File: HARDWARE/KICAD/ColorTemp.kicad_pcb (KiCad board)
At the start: 2 copper layers, 27.5 x 27.5 mm, 26 parts, among them J1 POWER, J2 Conn_02x05_Odd_Even, SW1 USER, SW2 ~{RESET}, U1 CH32V003F4U6, U2 MCP9700A

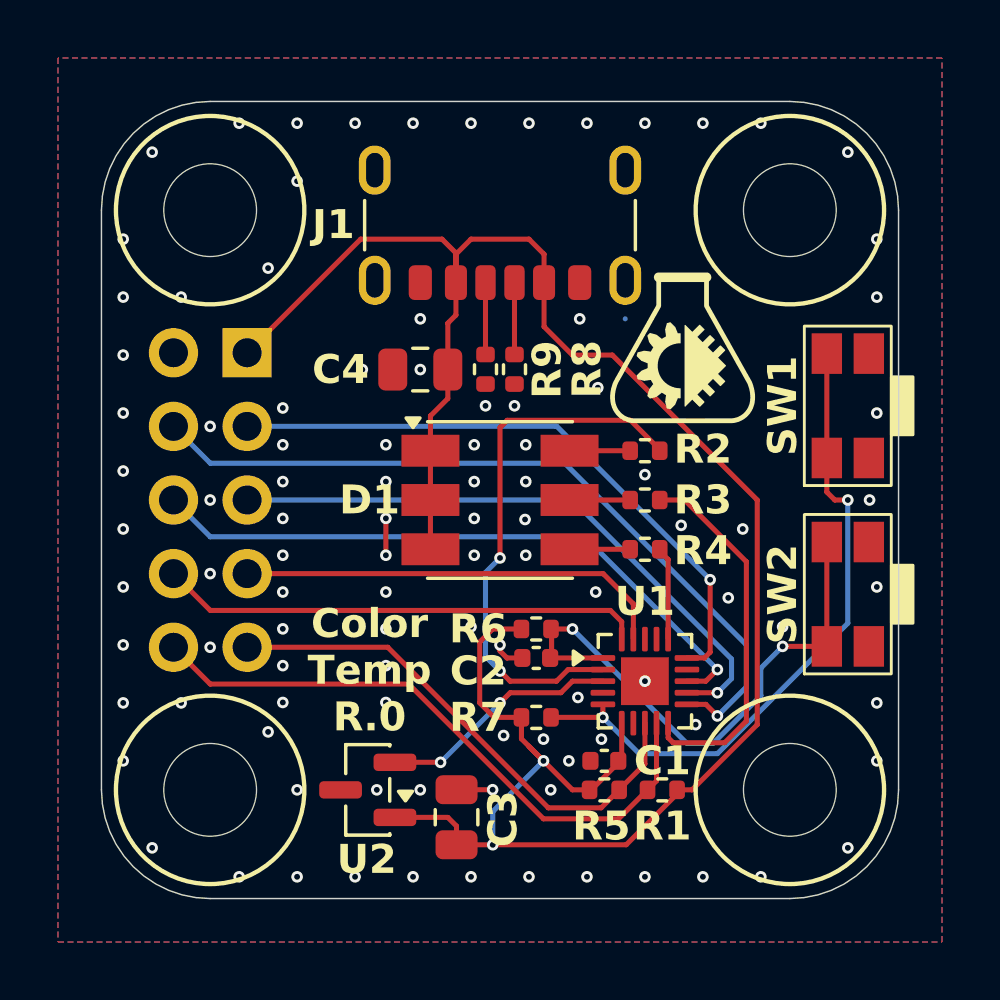
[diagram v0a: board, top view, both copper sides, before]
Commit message: Added fiducial marks.
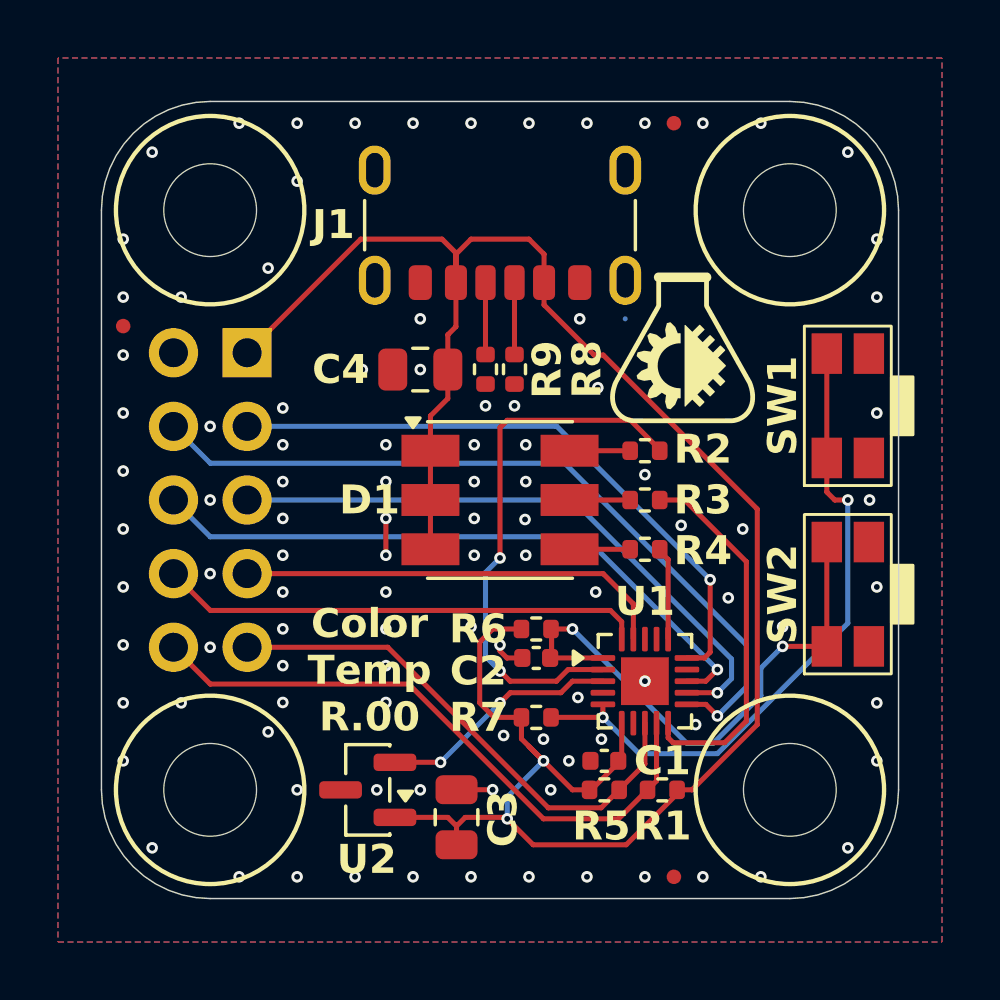
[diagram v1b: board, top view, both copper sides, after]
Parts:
- added FID1: Fiducial, ColorTemp:Fiducial_0.5mm_Mask1mm, F.Cu at (137.0, 94.0)
- added FID2: Fiducial, ColorTemp:Fiducial_0.5mm_Mask1mm, F.Cu at (156.0, 87.0)
- added FID3: Fiducial, ColorTemp:Fiducial_0.5mm_Mask1mm, F.Cu at (156.0, 113.0)
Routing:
- net +5V: track 75.8 -> 74.8 mm
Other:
- board text added: "Color Temp R.00"
- board text removed: "Color Temp R.0"

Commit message: Renumbering, PWR_FLAG, schematic detailing.
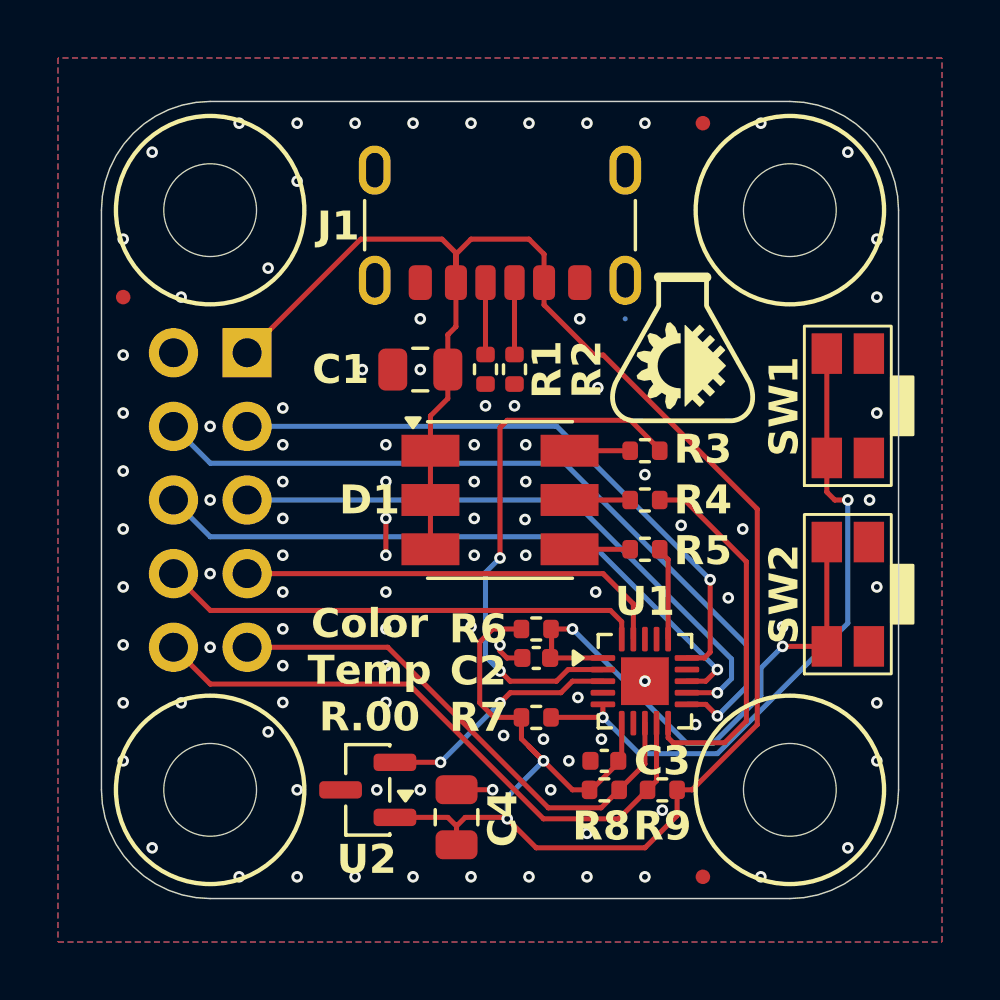
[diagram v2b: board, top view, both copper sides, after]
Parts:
- J2: value Conn_02x05_Odd_Even -> EXPANSION
- moved FID1 1.00 mm to (157.0, 87.0)
- moved FID2 1.00 mm to (137.0, 93.0)
- moved FID3 1.00 mm to (157.0, 113.0)
- moved G*** 0.57 mm to (153.8, 100.0), turned to -90 degrees
- renumbered C4 to C1, C1 to C3, C3 to C4, FID2 to FID1, FID1 to FID2, H3 to H1, H1 to H2, H4 to H3, H2 to H4, R9 to R1, R8 to R2, R2 to R3, R3 to R4, R4 to R5, R5 to R8, R1 to R9
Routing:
- net +5V: track 74.8 -> 75.3 mm
- net GND: vias 102 -> 101
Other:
- board text added: "C4 DIO"
- board text added: "C6 C5"
- board text added: "CL DA"
- board text added: "G 5V"
- board text added: "RX TX"
- board text removed: "5V G"
- board text removed: "C5 C6"
- board text removed: "DA CL"
- board text removed: "DIO C4"
- board text removed: "TX RX"

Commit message: Finished schematic.
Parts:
- R3, R4, R5: value 1K 1% -> 220R 1%
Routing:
- net GND: track 5.88 -> 5.79 mm, vias 101 -> 110
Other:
- board text added: "Mechatronix Lab Rev.00 2026.03.21"
- board text removed: "Mechatronix Lab Rev.00 2026.03.14"

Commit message: Finished Schematic and PCB Design.
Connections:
- net Net-(J1-CC1) renamed /CC1
- net Net-(J1-CC2) renamed /CC2
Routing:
- net GND: vias 110 -> 111
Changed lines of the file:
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@@
 	(net 18 "PC5")
 	(net 19 "USER")
-	(net 20 "Net-(J1-CC2)")
-	(net 21 "Net-(J1-CC1)")
+	(net 20 "/CC2")
+	(net 21 "/CC1")
 	(net 22 "unconnected-(U1-PD3-Pad17)")
 	(net 23 "unconnected-(U1-PC7-Pad14)")
@@
 			(end 2.5 -2.75)
 			(stroke
-				(width 0.1)
-				(type default)
+				(width 0.12)
+				(type solid)
 			)
 			(layer "F.SilkS")
@@
 		(fp_line
 			(start -2.5 2.75)
-			(end 2.5 2.75)
+			(end 3.65 2.75)
 			(stroke
-				(width 0.1)
-				(type default)
+				(width 0.12)
+				(type solid)
 			)
 			(layer "F.SilkS")
@@
 			)
 			(stroke
-				(width 0.1)
+				(width 0.12)
 				(type solid)
 			)
@@
 			)
 			(stroke
-				(width 0.1)
+				(width 0.12)
 				(type solid)
 			)
@@
 			)
 			(stroke
-				(width 0.1)
+				(width 0.12)
 				(type solid)
 			)
@@
 		(property "Reference" "SW2"
 			(at 0 -2.2 90)
-			(layer "F.SilkS" knockout)
+			(layer "F.SilkS")
 			(effects
 				(font
@@
 			(end 2.75 1.5)
 			(stroke
-				(width 0.1)
-				(type default)
+				(width 0.12)
+				(type solid)
 			)
 			(fill no)
@@
 		(property "Reference" "SW1"
 			(at -0.025 -2.2 90)
-			(layer "F.SilkS" knockout)
+			(layer "F.SilkS")
 			(effects
 				(font
@@
 			(end 2.75 1.5)
 			(stroke
-				(width 0.1)
-				(type default)
+				(width 0.12)
+				(type solid)
 			)
 			(fill no)
@@
 			(at 5.58 -1.13 0)
 			(unlocked yes)
-			(layer "F.SilkS" knockout)
+			(layer "F.SilkS")
 			(effects
 				(font
@@
 			(layers "F.Cu" "F.Mask" "F.Paste")
 			(roundrect_rratio 0.25)
-			(net 21 "Net-(J1-CC1)")
+			(net 21 "/CC1")
 			(pinfunction "CC1")
 			(pintype "bidirectional")
@@
 			(layers "F.Cu" "F.Mask" "F.Paste")
 			(roundrect_rratio 0.25)
-			(net 20 "Net-(J1-CC2)")
+			(net 20 "/CC2")
 			(pinfunction "CC2")
 			(pintype "bidirectional")
@@
 			(layers "F.Cu" "F.Mask" "F.Paste")
 			(roundrect_rratio 0.25)
-			(net 20 "Net-(J1-CC2)")
+			(net 20 "/CC2")
 			(pintype "passive")
 		)
@@
 			(end 3.25 0)
 			(stroke
-				(width 0.15)
+				(width 0.12)
 				(type solid)
 			)
@@
 			(layers "F.Cu" "F.Mask" "F.Paste")
 			(roundrect_rratio 0.25)
-			(net 21 "Net-(J1-CC1)")
+			(net 21 "/CC1")
 			(pintype "passive")
 		)
@@
 			(end 3.25 0)
 			(stroke
-				(width 0.15)
+				(width 0.12)
 				(type solid)
 			)
@@
 			(end 3.25 0)
 			(stroke
-				(width 0.15)
+				(width 0.12)
 				(type solid)
 			)
@@
 			(end 3.25 0)
 			(stroke
-				(width 0.15)
+				(width 0.12)
 				(type solid)
 			)
@@
 		(property "Reference" "J2"
 			(at -2.121 2.159 90)
-			(layer "B.SilkS" knockout)
+			(layer "B.SilkS")
 			(effects
 				(font
@@
 	)
 	(segment
-		(start 156.624548 110)
-		(end 156.22 110)
-		(width 0.175)
-		(layer "F.Cu")
-		(net 5)
-	)
-	(segment
 		(start 151.25 112)
 		(end 155 112)
@@
 	)
 	(segment
-		(start 153.5625 95)
-		(end 158.875 100.3125)
-		(width 0.175)
-		(layer "F.Cu")
-		(net 5)
-	)
-	(segment
 		(start 153.15 110)
 		(end 153.09 110)
@@
 	)
 	(segment
-		(start 151 91)
-		(end 151.52 91.52)
-		(width 0.175)
-		(layer "F.Cu")
-		(net 5)
-	)
-	(segment
 		(start 148.2 96.5)
 		(end 147.6 97.1)
@@
 	)
 	(segment
-		(start 151.52 93.27)
-		(end 153.25 95)
-		(width 0.175)
-		(layer "F.Cu")
-		(net 5)
-	)
-	(segment
 		(start 154.08 109.07)
 		(end 153.15 110)
@@
 	)
 	(segment
-		(start 151.5 109)
-		(end 150.74 108.24)
+		(start 156.624548 110)
+		(end 156.22 110)
 		(width 0.175)
 		(layer "F.Cu")
@@
 	)
 	(segment
-		(start 158.875 107.749548)
-		(end 156.624548 110)
+		(start 151.5 109)
+		(end 150.74 108.24)
 		(width 0.175)
 		(layer "F.Cu")
@@
 	)
 	(segment
-		(start 148.8 110.95)
-		(end 148.5 111.25)
+		(start 156.11 109.89)
+		(end 156.11 110)
 		(width 0.175)
 		(layer "F.Cu")
@@
 	)
 	(segment
-		(start 156.11 109.89)
-		(end 156.11 110)
+		(start 148.8 110.95)
+		(end 148.5 111.25)
 		(width 0.175)
 		(layer "F.Cu")
@@
 	)
 	(segment
-		(start 156.22 110)
-		(end 156.11 109.89)
+		(start 148.48 92.58)
+		(end 148.48 92.5)
 		(width 0.175)
 		(layer "F.Cu")
@@
 	)
 	(segment
-		(start 148.48 92.58)
-		(end 148.48 92.5)
+		(start 153.78125 95)
+		(end 158.875 100.09375)
 		(width 0.175)
 		(layer "F.Cu")
@@
 	)
 	(segment
-		(start 153.25 95)
-		(end 153.5625 95)
+		(start 151.52 91.52)
+		(end 151.52 93.52)
 		(width 0.175)
 		(layer "F.Cu")
@@
 	)
 	(segment
+		(start 149 91)
+		(end 151 91)
+		(width 0.175)
+		(layer "F.Cu")
+		(net 5)
+	)
+	(segment
+		(start 158.875 100.09375)
+		(end 158.875 107.749548)
+		(width 0.175)
+		(layer "F.Cu")
+		(net 5)
+	)
+	(segment
 		(start 150.74 108.24)
 		(end 150.74 107.5)
@@
 	)
 	(segment
-		(start 149 91)
-		(end 151 91)
+		(start 151 91)
+		(end 151.52 91.52)
 		(width 0.175)
 		(layer "F.Cu")
@@
 	)
 	(segment
-		(start 158.875 100.3125)
-		(end 158.875 107.749548)
+		(start 148.48 91.52)
+		(end 149 91)
+		(width 0.175)
+		(layer "F.Cu")
+		(net 5)
+	)
+	(segment
+		(start 156.22 110)
+		(end 156.11 109.89)
+		(width 0.175)
+		(layer "F.Cu")
+		(net 5)
+	)
+	(segment
+		(start 151.52 93.52)
+		(end 153 95)
 		(width 0.175)
 		(layer "F.Cu")
@@
 	)
 	(segment
-		(start 150.74 104.45)
-		(end 149.75 104.45)
-		(width 0.175)
-		(layer "F.Cu")
-		(net 5)
-	)
-	(segment
-		(start 148.48 91.52)
-		(end 149 91)
+		(start 153 95)
+		(end 153.78125 95)
 		(width 0.175)
 		(layer "F.Cu")
@@
 	)
 	(segment
-		(start 151.52 91.52)
-		(end 151.52 93.27)
+		(start 150.74 104.45)
+		(end 149.75 104.45)
 		(width 0.175)
 		(layer "F.Cu")
@@
 	)
 	(segment
+		(start 158.875 107.749548)
+		(end 156.624548 110)
+		(width 0.175)
+		(layer "F.Cu")
+		(net 5)
+	)
+	(segment
 		(start 155 112)
 		(end 156.11 110.89)
@@
 	)
 	(via
-		(at 153.375 96.125)
+		(at 152.75 95.5)
 		(size 0.4)
 		(drill 0.2)
@@
 	)
 	(via
-		(at 159.75 104.375)
+		(at 160.25 104.375)
 		(size 0.4)
 		(drill 0.2)
@@
 	)
 	(via
-		(at 155 99.125)
+		(at 154.5 99.125)
 		(size 0.4)
 		(drill 0.2)
@@
 		(net 6)
 	)
+	(via
+		(at 160.795 100)
+		(size 0.4)
+		(drill 0.2)
+		(layers "F.Cu" "B.Cu")
+		(free yes)
+		(net 6)
+	)
